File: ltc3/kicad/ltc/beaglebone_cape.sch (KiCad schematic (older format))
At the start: 11 parts, among them P501 BeagleBone_Black_Expansion_He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, P502 BeagleBone_Black_Expansion_He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, U501 24C256

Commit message: LTC3: Updates to LTC schematic.
1. Cleaned up top-level sheet.
2. Added board-to-board connectors for power, I2C.
3. Miscelleneous component part selection/changes.
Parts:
- removed R501, R502, R504: 5.6k, Resistors_SMD:R_0805, symbol R
- added P303: JST PH header, Connectors_JST:JST_PH_B2B-PH-K_02x2.00mm_Straight, symbol CONN_01X02
- added R301, R302, R304: 5.6k, Resistors_SMD:R_0603, symbol R
- C301: renamed from C501; Mfg_Name (none) -> -; Mfg_PN (none) -> -; Note (none) -> -; Spec (none) -> 5V
- R303: renamed from R503; footprint Resistors_SMD:R_0805 -> Resistors_SMD:R_0603; Mfg_Name (none) -> -; Mfg_PN (none) -> -; Note (none) -> -; Spec (none) -> -
- U301: renamed from U501; value 24C256 -> CAT24C256; Mfg_Name (none) -> ON; Mfg_PN (none) -> CAT24C256YI-GT3; Note (none) -> -; Spec (none) -> -
- renumbered JP501 to JP301, P501 to P301, P502 to P302, W501 to W301, W502 to W302
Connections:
- net +5V: now also R301.1, R302.1, R304.1
- net I2C_CLOCK: now also P303.2 (P2)
- net I2C_DATA: now also P303.1 (P1), R304.2
- net at U301.3 (A3): now also R302.2
- net at JP301.1, U301.7 (WP): now also R301.2
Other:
- moved on the sheet: W301, W302

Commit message: LTC3: Modified LTC BeagleBone cape schematic.
Replaced external I2C connector with combined I2C/5.0V connector.
Added a second connector in parallel, so that the charge controller
and cell protection boards each have their own.
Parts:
- added P304: JST PH header, Connectors_JST:JST_PH_B4B-PH-K_02x2.00mm_Straight, symbol CONN_01X04
- P303: footprint Connectors_JST:JST_PH_B2B-PH-K_02x2.00mm_Straight -> Connectors_JST:JST_PH_B4B-PH-K_02x2.00mm_Straight; symbol CONN_01X02 -> CONN_01X04; Mfg_PN B2B-PH-K-S -> B4B-PH-K-S; Note - -> To Charge Controller
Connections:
- net +5V: now also P303.1 (P1), P304.1 (P1)
- net I2C_CLOCK: now also P303.3 (P3), P304.3 (P3); no longer P303.2 (P2)
- net I2C_DATA: now also P303.2 (P2), P304.2 (P2); no longer P303.1 (P1)
- new net GNDREF: P303.4 (P4), P304.4 (P4)
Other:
- moved on the sheet: W301, W302
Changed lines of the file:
@@
 	15150 3400 15750 3400
 Wire Wire Line
-	15350 3150 15350 3800
+	15350 3150 15350 3250
+Wire Wire Line
+	15350 3250 15350 3800
 Wire Wire Line
 	15150 3250 15350 3250
@@
 	13650 3400 13500 3400
 Wire Wire Line
-	13500 3250 13500 4150
+	13500 3250 13500 3400
+Wire Wire Line
+	13500 3400 13500 4150
 Wire Wire Line
 	13650 3250 13500 3250
@@
 $EndComp
 Wire Wire Line
-	8150 5200 8150 5400
+	8150 5200 8150 5300
+Wire Wire Line
+	8150 5300 8150 5400
 Wire Wire Line
 	8150 5300 8400 5300
@@
 $EndComp
 Wire Wire Line
-	10550 5200 10550 5400
+	10550 5200 10550 5300
+Wire Wire Line
+	10550 5300 10550 5400
 Wire Wire Line
 	10550 5300 10300 5300
@@
 $EndComp
 Wire Wire Line
-	10800 2800 10800 3550
+	10800 2800 10800 3300
+Wire Wire Line
+	10800 3300 10800 3550
 $Comp
 L +5V #PWR305
@@
 $EndComp
 Wire Wire Line
-	7900 2800 7900 3550
+	7900 2800 7900 3300
+Wire Wire Line
+	7900 3300 7900 3550
 $Comp
 L +5V #PWR301
@@
 Connection ~ 7900 3300
 Wire Wire Line
-	7900 3850 7900 6050
+	7900 3850 7900 4000
+Wire Wire Line
+	7900 4000 7900 6050
 Connection ~ 10800 3300
 Wire Wire Line
-	10800 3850 10800 5100
+	10800 3850 10800 4000
+Wire Wire Line
+	10800 4000 10800 5100
 Wire Notes Line
 	950  2200 11800 2200
@@
 Text Notes 950  6900 0    100  ~ 0
 BeagleBone Expansion Headers
-Text HLabel 14300 6300 0    50   BiDi ~ 0
+Text HLabel 14100 6300 0    50   BiDi ~ 0
 I2C_CLOCK
-Text HLabel 14300 6200 0    50   BiDi ~ 0
+Text HLabel 14100 6200 0    50   BiDi ~ 0
 I2C_DATA
 Text HLabel 1850 4200 0    60   Input ~ 0
@@
 	15650 3550 15650 5100
 Wire Wire Line
-	15650 5100 10800 5100
+	15650 5100 14700 5100
+Wire Wire Line
+	14700 5100 10800 5100
 Wire Wire Line
 	7900 6050 10800 6050
 Wire Wire Line
-	15750 5200 10800 5200
+	15750 5200 14800 5200
+Wire Wire Line
+	14800 5200 10800 5200
 Wire Wire Line
 	10800 5200 10800 6050
@@
 L TEST W302
 U 1 1 56C9D70E
-P 14650 6650
-F 0 "W302" H 14650 6750 50  0000 C CNN
-F 1 "TEST" H 14650 6580 50  0001 C CNN
-F 2 "Measurement_Points:Test_Point_2Pads" H 14650 6650 50  0001 C CNN
-F 3 "" H 14650 6650 50  0000 C CNN
-	1    14650 6650
-	0    1    1    0
-$EndComp
-$Comp
-L GND #PWR318
-U 1 1 56C9D74D
-P 14650 6900
-F 0 "#PWR318" H 14650 6650 50  0001 C CNN
-F 1 "GND" H 14650 6750 50  0001 C CNN
-F 2 "" H 14650 6900 50  0000 C CNN
-F 3 "" H 14650 6900 50  0000 C CNN
-	1    14650 6900
-	1    0    0    -1
-$EndComp
-Wire Wire Line
-	14650 6900 14650 6850
-$Comp
-L TEST W301
-U 1 1 56C9D96C
 P 14450 6650
-F 0 "W301" H 14450 6750 50  0000 C CNN
+F 0 "W302" H 14450 6750 50  0000 C CNN
 F 1 "TEST" H 14450 6580 50  0001 C CNN
 F 2 "Measurement_Points:Test_Point_2Pads" H 14450 6650 50  0001 C CNN
@@
 $EndComp
 $Comp
-L GND #PWR317
-U 1 1 56C9D9B3
+L GND #PWR320
+U 1 1 56C9D74D
 P 14450 6900
-F 0 "#PWR317" H 14450 6650 50  0001 C CNN
+F 0 "#PWR320" H 14450 6650 50  0001 C CNN
 F 1 "GND" H 14450 6750 50  0001 C CNN
 F 2 "" H 14450 6900 50  0000 C CNN
@@
 Wire Wire Line
 	14450 6900 14450 6850
+$Comp
+L TEST W301
+U 1 1 56C9D96C
+P 14250 6650
+F 0 "W301" H 14250 6750 50  0000 C CNN
+F 1 "TEST" H 14250 6580 50  0001 C CNN
+F 2 "Measurement_Points:Test_Point_2Pads" H 14250 6650 50  0001 C CNN
+F 3 "" H 14250 6650 50  0000 C CNN
+	1    14250 6650
+	0    1    1    0
+$EndComp
+$Comp
+L GND #PWR319
+U 1 1 56C9D9B3
+P 14250 6900
+F 0 "#PWR319" H 14250 6650 50  0001 C CNN
+F 1 "GND" H 14250 6750 50  0001 C CNN
+F 2 "" H 14250 6900 50  0000 C CNN
+F 3 "" H 14250 6900 50  0000 C CNN
+	1    14250 6900
+	1    0    0    -1
+$EndComp
+Wire Wire Line
+	14250 6900 14250 6850
 Wire Notes Line
 	750  9250 750  10250
@@
 $EndComp
 $Comp
-L CONN_01X02 P303
+L CONN_01X04 P303
 U 1 1 5773408D
-P 15350 6250
-F 0 "P303" H 15350 6400 50  0000 C CNN
-F 1 "JST PH header" V 15500 6250 50  0000 C CNN
-F 2 "Connectors_JST:JST_PH_B2B-PH-K_02x2.00mm_Straight" H 15350 6250 50  0001 C CNN
-F 3 "https://github.com/psas/launch-tower/blob/master/ltc3/doc/datasheets/connectors/JST-PH_connector.pdf" H 15350 6250 50  0001 C CNN
-F 4 "-" H 15350 6250 60  0001 C CNN "Spec"
-F 5 "-" H 15350 6250 60  0001 C CNN "Note"
-F 6 "JST" H 15350 6250 60  0001 C CNN "Mfg_Name"
-F 7 "B2B-PH-K-S" H 15350 6250 60  0001 C CNN "Mfg_PN"
-	1    15350 6250
-	1    0    0    -1
-$EndComp
-Wire Wire Line
-	14300 6200 15150 6200
-Wire Wire Line
-	14300 6300 15150 6300
-Wire Wire Line
-	14450 6450 14450 6200
-Connection ~ 14450 6200
+P 15800 6250
+F 0 "P303" H 15800 6500 50  0000 C CNN
+F 1 "JST PH header" V 15950 6250 50  0000 C CNN
+F 2 "Connectors_JST:JST_PH_B4B-PH-K_02x2.00mm_Straight" H 15800 6250 50  0001 C CNN
+F 3 "https://github.com/psas/launch-tower/blob/master/ltc3/doc/datasheets/connectors/JST-PH_connector.pdf" H 15800 6250 50  0001 C CNN
+F 4 "-" H 15800 6250 60  0001 C CNN "Spec"
+F 5 "To Charge Controller" V 16050 6250 50  0000 C CNN "Note"
+F 6 "JST" H 15800 6250 60  0001 C CNN "Mfg_Name"
+F 7 "B4B-PH-K-S" H 15800 6250 60  0001 C CNN "Mfg_PN"
+	1    15800 6250
+	1    0    0    -1
+$EndComp
+Wire Wire Line
+	14100 6200 14250 6200
+Wire Wire Line
+	14250 6200 14700 6200
+Wire Wire Line
+	14700 6200 14950 6200
+Wire Wire Line
+	14950 6200 15600 6200
+Wire Wire Line
+	14100 6300 14450 6300
+Wire Wire Line
+	14450 6300 14800 6300
+Wire Wire Line
+	14800 6300 15050 6300
+Wire Wire Line
+	15050 6300 15600 6300
+Wire Wire Line
+	14250 6450 14250 6200
+Connection ~ 14250 6200
 Wire Wire Line
 	10800 4000 10300 4000
@@
 	8400 4000 7900 4000
 Wire Wire Line
-	14650 6450 14650 6300
-Connection ~ 14650 6300
-Wire Wire Line
-	15000 6300 15000 5200
-Connection ~ 15000 5200
-Connection ~ 15000 6300
-Wire Wire Line
-	14900 6200 14900 5100
-Connection ~ 14900 5100
-Connection ~ 14900 6200
+	14450 6450 14450 6300
+Connection ~ 14450 6300
+Wire Wire Line
+	14800 6300 14800 5200
+Connection ~ 14800 5200
+Connection ~ 14800 6300
+Wire Wire Line
+	14700 6200 14700 5100
+Connection ~ 14700 5100
+Connection ~ 14700 6200
 $Comp
 L R R302
@@
 	1    0    0    -1
 $EndComp
+$Comp
+L GNDREF #PWR318
+U 1 1 57D1A6B8
+P 15450 6550
+F 0 "#PWR318" H 15450 6300 50  0001 C CNN
+F 1 "GNDREF" H 15450 6400 50  0001 C CNN
+F 2 "" H 15450 6550 50  0000 C CNN
+F 3 "" H 15450 6550 50  0000 C CNN
+	1    15450 6550
+	1    0    0    -1
+$EndComp
+Wire Wire Line
+	15450 6550 15450 6400
+Wire Wire Line
+	15450 6400 15600 6400
+$Comp
+L +5V #PWR317
+U 1 1 57D1A803
+P 15450 5950
+F 0 "#PWR317" H 15450 5800 50  0001 C CNN
+F 1 "+5V" H 15450 6090 50  0000 C CNN
+F 2 "" H 15450 5950 50  0000 C CNN
+F 3 "" H 15450 5950 50  0000 C CNN
+	1    15450 5950
+	1    0    0    -1
+$EndComp
+Wire Wire Line
+	15450 5950 15450 6100
+Wire Wire Line
+	15450 6100 15600 6100
+$Comp
+L CONN_01X04 P304
+U 1 1 57D1AB59
+P 15800 7350
+F 0 "P304" H 15800 7600 50  0000 C CNN
+F 1 "JST PH header" V 15950 7350 50  0000 C CNN
+F 2 "Connectors_JST:JST_PH_B4B-PH-K_02x2.00mm_Straight" H 15800 7350 50  0001 C CNN
+F 3 "https://github.com/psas/launch-tower/blob/master/ltc3/doc/datasheets/connectors/JST-PH_connector.pdf" H 15800 7350 50  0001 C CNN
+F 4 "-" H 15800 7350 60  0001 C CNN "Spec"
+F 5 "To Cell Protection" V 16050 7350 50  0000 C CNN "Note"
+F 6 "JST" H 15800 7350 60  0001 C CNN "Mfg_Name"
+F 7 "B4B-PH-K-S" H 15800 7350 60  0001 C CNN "Mfg_PN"
+	1    15800 7350
+	1    0    0    -1
+$EndComp
+Wire Wire Line
+	14950 7300 15600 7300
+Wire Wire Line
+	15050 7400 15600 7400
+$Comp
+L GNDREF #PWR322
+U 1 1 57D1AB61
+P 15450 7650
+F 0 "#PWR322" H 15450 7400 50  0001 C CNN
+F 1 "GNDREF" H 15450 7500 50  0001 C CNN
+F 2 "" H 15450 7650 50  0000 C CNN
+F 3 "" H 15450 7650 50  0000 C CNN
+	1    15450 7650
+	1    0    0    -1
+$EndComp
+Wire Wire Line
+	15450 7650 15450 7500
+Wire Wire Line
+	15450 7500 15600 7500
+$Comp
+L +5V #PWR321
+U 1 1 57D1AB69
+P 15450 7050
+F 0 "#PWR321" H 15450 6900 50  0001 C CNN
+F 1 "+5V" H 15450 7190 50  0000 C CNN
+F 2 "" H 15450 7050 50  0000 C CNN
+F 3 "" H 15450 7050 50  0000 C CNN
+	1    15450 7050
+	1    0    0    -1
+$EndComp
+Wire Wire Line
+	15450 7050 15450 7200
+Wire Wire Line
+	15450 7200 15600 7200
+Wire Wire Line
+	14950 7300 14950 6200
+Connection ~ 14950 6200
+Wire Wire Line
+	15050 7400 15050 6300
+Connection ~ 15050 6300
 $EndSCHEMATC

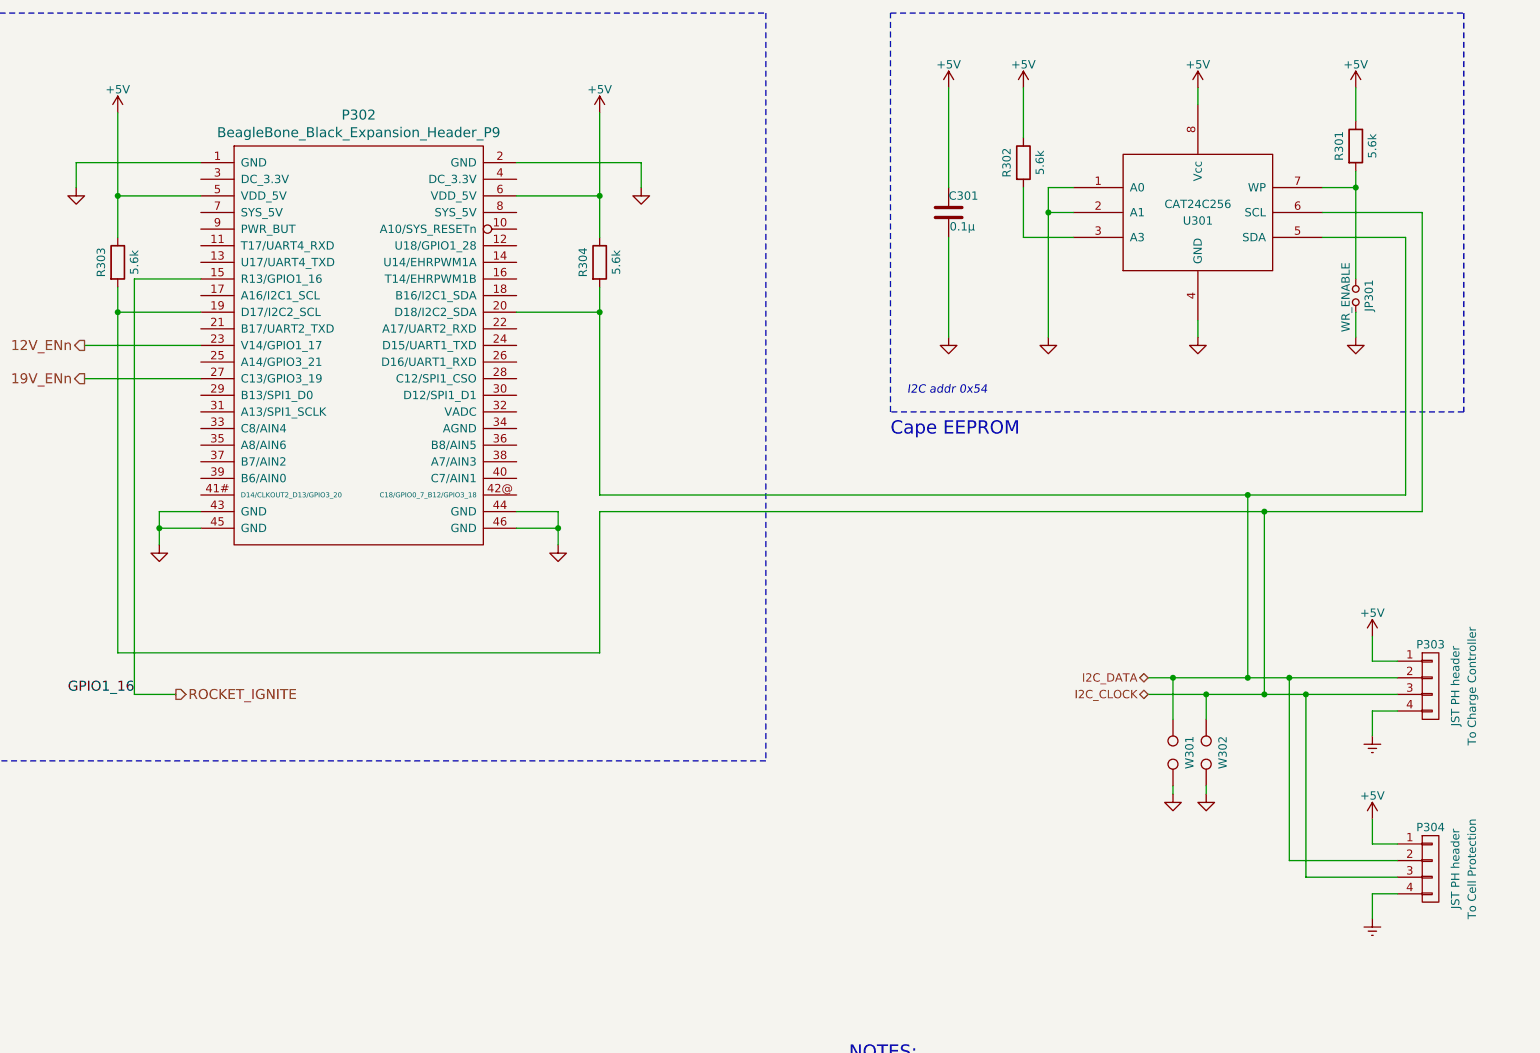
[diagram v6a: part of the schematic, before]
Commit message: LTC3: Modified LTC BeagleBone cape schematic.
Changed GNDREF symbols on external low-voltage/I2C connectors to
primary ground.  Only the charge controller and cell protection boards
need a separate low-voltage ground node.
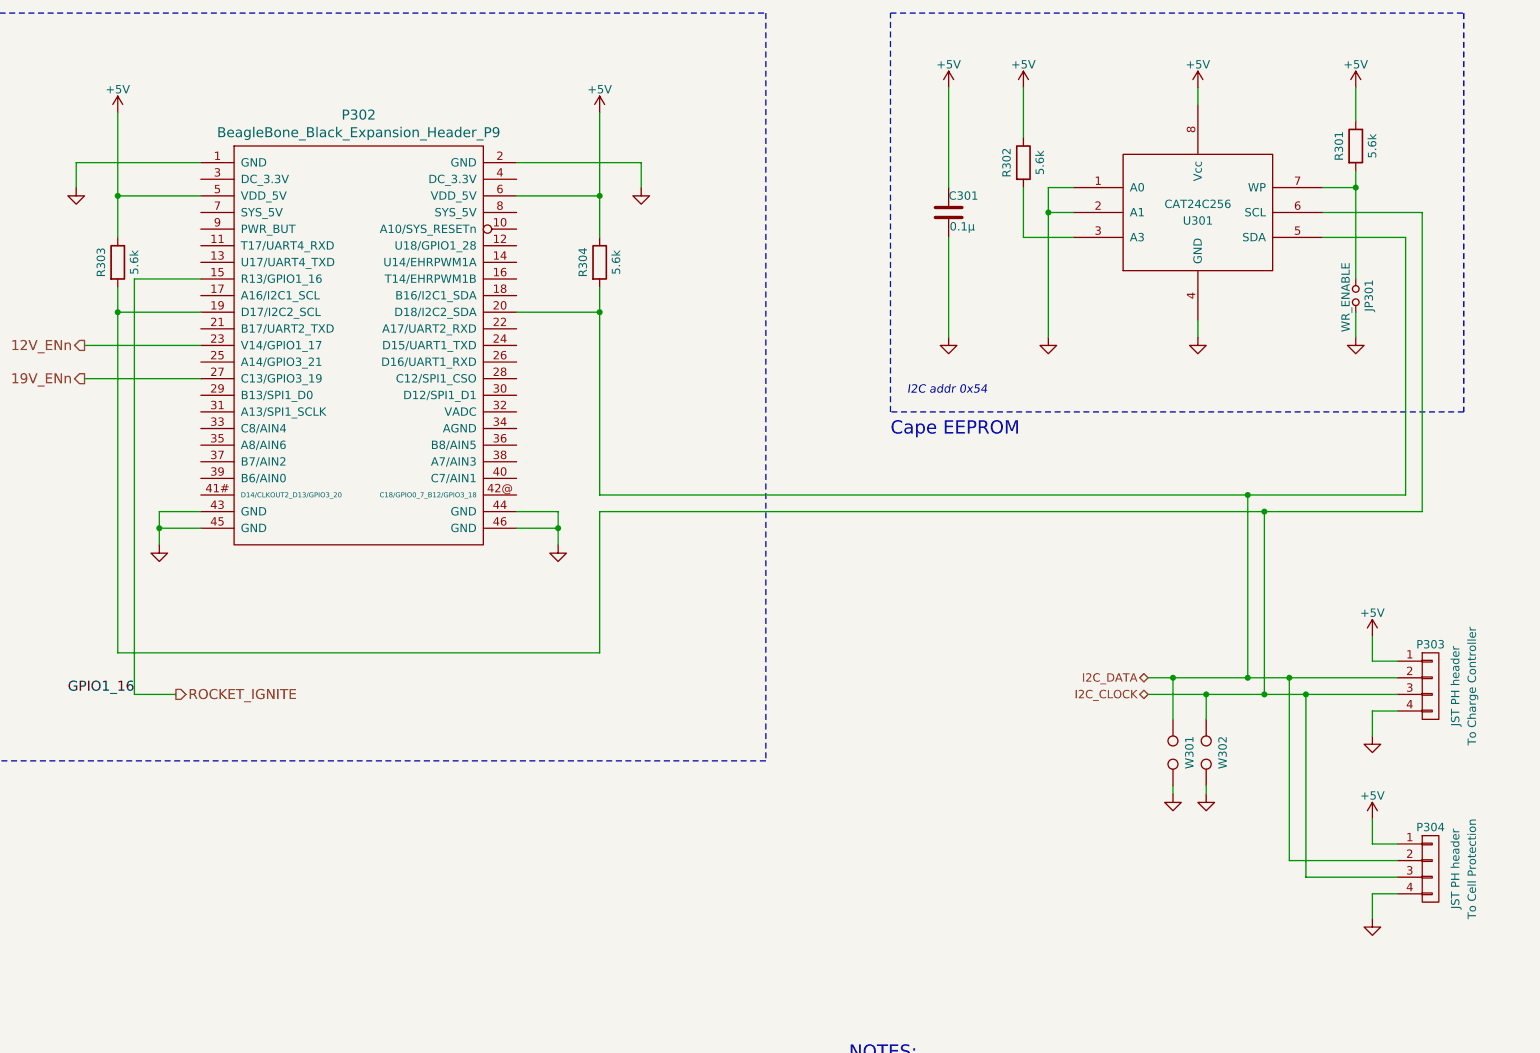
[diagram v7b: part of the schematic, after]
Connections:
- net GNDREF is gone; now on net GND: P303.4 (P4), P304.4 (P4)
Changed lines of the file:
@@
 EXT_PWR_EN_4
-$Comp
-L GND #PWR313
-U 1 1 557C941A
-P 14400 4150
-F 0 "#PWR313" H 14400 3900 50  0001 C CNN
-F 1 "GND" H 14400 4000 50  0001 C CNN
-F 2 "" H 14400 4150 60  0000 C CNN
-F 3 "" H 14400 4150 60  0000 C CNN
-	1    14400 4150
-	1    0    0    -1
-$EndComp
 $Comp
 L Jumper_NO_Small JP301
@@
 	0    1    1    0
 $EndComp
-$Comp
-L GND #PWR314
-U 1 1 557CCCE2
-P 15350 4150
-F 0 "#PWR314" H 15350 3900 50  0001 C CNN
-F 1 "GND" H 15350 4000 50  0001 C CNN
-F 2 "" H 15350 4150 60  0000 C CNN
-F 3 "" H 15350 4150 60  0000 C CNN
-	1    15350 4150
-	1    0    0    -1
-$EndComp
-$Comp
-L GND #PWR312
-U 1 1 557CCE7C
-P 13500 4150
-F 0 "#PWR312" H 13500 3900 50  0001 C CNN
-F 1 "GND" H 13500 4000 50  0001 C CNN
-F 2 "" H 13500 4150 60  0000 C CNN
-F 3 "" H 13500 4150 60  0000 C CNN
-	1    13500 4150
-	1    0    0    -1
-$EndComp
-$Comp
-L GND #PWR311
-U 1 1 557CE60A
-P 12900 4150
-F 0 "#PWR311" H 12900 3900 50  0001 C CNN
-F 1 "GND" H 12900 4000 50  0001 C CNN
-F 2 "" H 12900 4150 60  0000 C CNN
-F 3 "" H 12900 4150 60  0000 C CNN
-	1    12900 4150
-	1    0    0    -1
-$EndComp
 Text HLabel 7700 4200 0    60   Output ~ 0
 12V_ENn
@@
 	15150 3400 15750 3400
 Wire Wire Line
-	15350 3150 15350 3250
-Wire Wire Line
-	15350 3250 15350 3800
+	15350 3150 15350 3800
 Wire Wire Line
 	15150 3250 15350 3250
@@
 	13650 3400 13500 3400
 Wire Wire Line
-	13500 3250 13500 3400
-Wire Wire Line
-	13500 3400 13500 4150
+	13500 3250 13500 4150
 Wire Wire Line
 	13650 3250 13500 3250
@@
 $EndComp
 Wire Wire Line
-	8150 5200 8150 5300
-Wire Wire Line
-	8150 5300 8150 5400
+	8150 5200 8150 5400
 Wire Wire Line
 	8150 5300 8400 5300
@@
 $EndComp
 Wire Wire Line
-	10550 5200 10550 5300
-Wire Wire Line
-	10550 5300 10550 5400
+	10550 5200 10550 5400
 Wire Wire Line
 	10550 5300 10300 5300
@@
 $EndComp
 Wire Wire Line
-	10800 2800 10800 3300
-Wire Wire Line
-	10800 3300 10800 3550
+	10800 2800 10800 3550
 $Comp
 L +5V #PWR305
@@
 $EndComp
 Wire Wire Line
-	7900 2800 7900 3300
-Wire Wire Line
-	7900 3300 7900 3550
+	7900 2800 7900 3550
 $Comp
 L +5V #PWR301
@@
 Connection ~ 7900 3300
 Wire Wire Line
-	7900 3850 7900 4000
-Wire Wire Line
-	7900 4000 7900 6050
+	7900 3850 7900 6050
 Connection ~ 10800 3300
 Wire Wire Line
-	10800 3850 10800 4000
-Wire Wire Line
-	10800 4000 10800 5100
+	10800 3850 10800 5100
 Wire Notes Line
 	950  2200 11800 2200
@@
 ROCKET_IGNITE
 Wire Wire Line
-	15750 3400 15750 5200
-Wire Wire Line
-	15650 3550 15650 5100
-Wire Wire Line
-	15650 5100 14700 5100
-Wire Wire Line
-	14700 5100 10800 5100
+	15750 5200 15750 3400
+Wire Wire Line
+	15650 5100 15650 3550
+Wire Wire Line
+	10800 5100 15650 5100
 Wire Wire Line
 	7900 6050 10800 6050
 Wire Wire Line
-	15750 5200 14800 5200
-Wire Wire Line
-	14800 5200 10800 5200
-Wire Wire Line
-	10800 5200 10800 6050
+	10800 5200 15750 5200
+Wire Wire Line
+	10800 6050 10800 5200
 Connection ~ 7900 4000
 Wire Wire Line
@@
 $EndComp
 Wire Wire Line
-	14100 6200 14250 6200
-Wire Wire Line
-	14250 6200 14700 6200
-Wire Wire Line
-	14700 6200 14950 6200
-Wire Wire Line
-	14950 6200 15600 6200
-Wire Wire Line
-	14100 6300 14450 6300
-Wire Wire Line
-	14450 6300 14800 6300
-Wire Wire Line
-	14800 6300 15050 6300
-Wire Wire Line
-	15050 6300 15600 6300
+	14100 6200 15600 6200
+Wire Wire Line
+	14100 6300 15600 6300
 Wire Wire Line
 	14250 6450 14250 6200
@@
 $EndComp
 $Comp
-L GNDREF #PWR318
+L GND #PWR318
 U 1 1 57D1A6B8
 P 15450 6550
 F 0 "#PWR318" H 15450 6300 50  0001 C CNN
-F 1 "GNDREF" H 15450 6400 50  0001 C CNN
+F 1 "GND" H 15450 6400 50  0001 C CNN
 F 2 "" H 15450 6550 50  0000 C CNN
 F 3 "" H 15450 6550 50  0000 C CNN
+F 4 "-" H 15450 6550 60  0001 C CNN "Spec"
+F 5 "-" H 15450 6550 60  0001 C CNN "Note"
+F 6 "-" H 15450 6550 60  0001 C CNN "Mfg_Name"
+F 7 "-" H 15450 6550 60  0001 C CNN "Mfg_PN"
 	1    15450 6550
 	1    0    0    -1
@@
 	15050 7400 15600 7400
 $Comp
-L GNDREF #PWR322
+L GND #PWR322
 U 1 1 57D1AB61
 P 15450 7650
 F 0 "#PWR322" H 15450 7400 50  0001 C CNN
-F 1 "GNDREF" H 15450 7500 50  0001 C CNN
+F 1 "GND" H 15450 7500 50  0001 C CNN
 F 2 "" H 15450 7650 50  0000 C CNN
 F 3 "" H 15450 7650 50  0000 C CNN
+F 4 "-" H 15450 7650 60  0001 C CNN "Spec"
+F 5 "-" H 15450 7650 60  0001 C CNN "Note"
+F 6 "-" H 15450 7650 60  0001 C CNN "Mfg_Name"
+F 7 "-" H 15450 7650 60  0001 C CNN "Mfg_PN"
 	1    15450 7650
 	1    0    0    -1
@@
 	15050 7400 15050 6300
 Connection ~ 15050 6300
+$Comp
+L GND #PWR312
+U 1 1 557CCE7C
+P 13500 4150
+F 0 "#PWR312" H 13500 3900 50  0001 C CNN
+F 1 "GND" H 13500 4000 50  0001 C CNN
+F 2 "" H 13500 4150 60  0000 C CNN
+F 3 "" H 13500 4150 60  0000 C CNN
+	1    13500 4150
+	1    0    0    -1
+$EndComp
+$Comp
+L GND #PWR314
+U 1 1 557CCCE2
+P 15350 4150
+F 0 "#PWR314" H 15350 3900 50  0001 C CNN
+F 1 "GND" H 15350 4000 50  0001 C CNN
+F 2 "" H 15350 4150 60  0000 C CNN
+F 3 "" H 15350 4150 60  0000 C CNN
+	1    15350 4150
+	1    0    0    -1
+$EndComp
+$Comp
+L GND #PWR313
+U 1 1 557C941A
+P 14400 4150
+F 0 "#PWR313" H 14400 3900 50  0001 C CNN
+F 1 "GND" H 14400 4000 50  0001 C CNN
+F 2 "" H 14400 4150 60  0000 C CNN
+F 3 "" H 14400 4150 60  0000 C CNN
+	1    14400 4150
+	1    0    0    -1
+$EndComp
+$Comp
+L GND #PWR311
+U 1 1 557CE60A
+P 12900 4150
+F 0 "#PWR311" H 12900 3900 50  0001 C CNN
+F 1 "GND" H 12900 4000 50  0001 C CNN
+F 2 "" H 12900 4150 60  0000 C CNN
+F 3 "" H 12900 4150 60  0000 C CNN
+	1    12900 4150
+	1    0    0    -1
+$EndComp
 $EndSCHEMATC
